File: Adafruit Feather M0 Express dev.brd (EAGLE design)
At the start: 50.8 x 22.9 mm, 41 parts, among them J2 AVR_SPI_PROG_3X2PTH, SW1 SPST_TACT-KMR2, U1 2MB Flash, U2 AP2112-3.3, U3 MCP73831T-2ACI/OT, X1 JSTPH, X2 32.768, X3 microUSB, X4 2x5 0.05" SWD

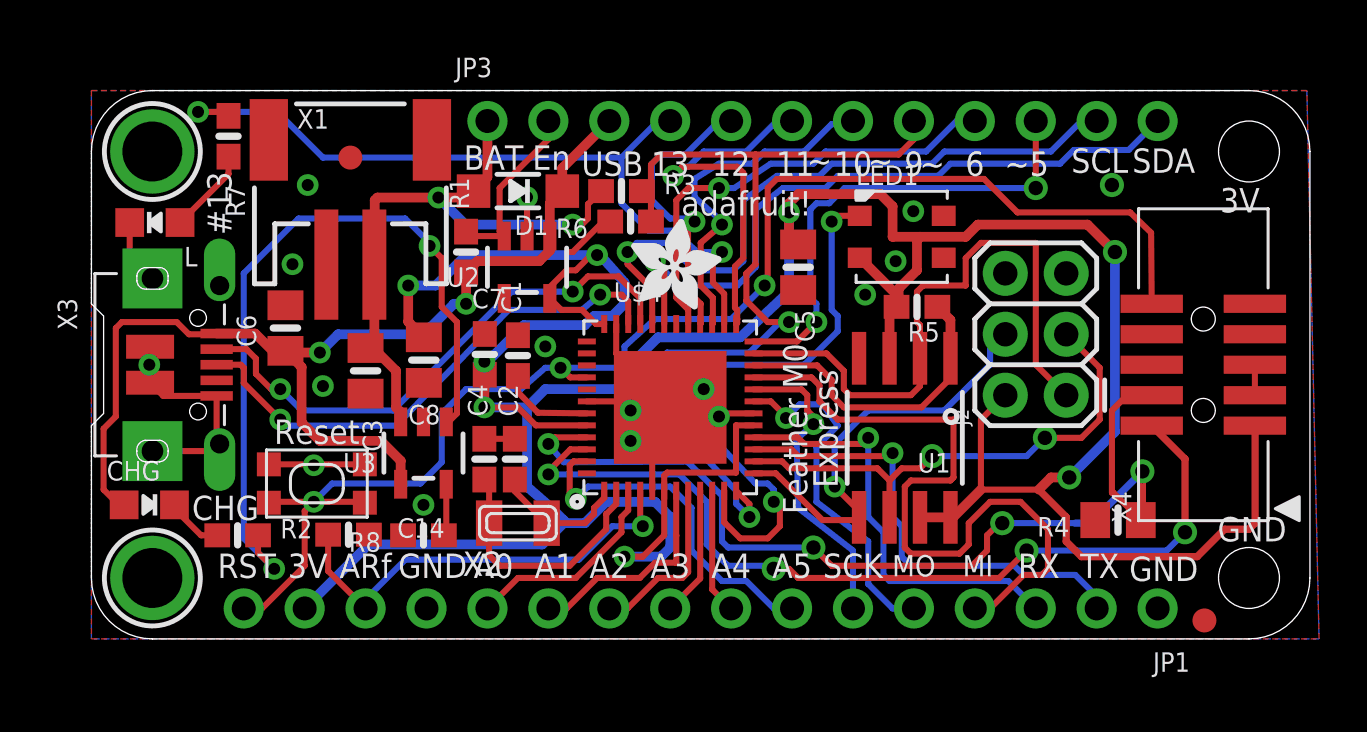
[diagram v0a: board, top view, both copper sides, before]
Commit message: fixed all bottom layer DRC errors
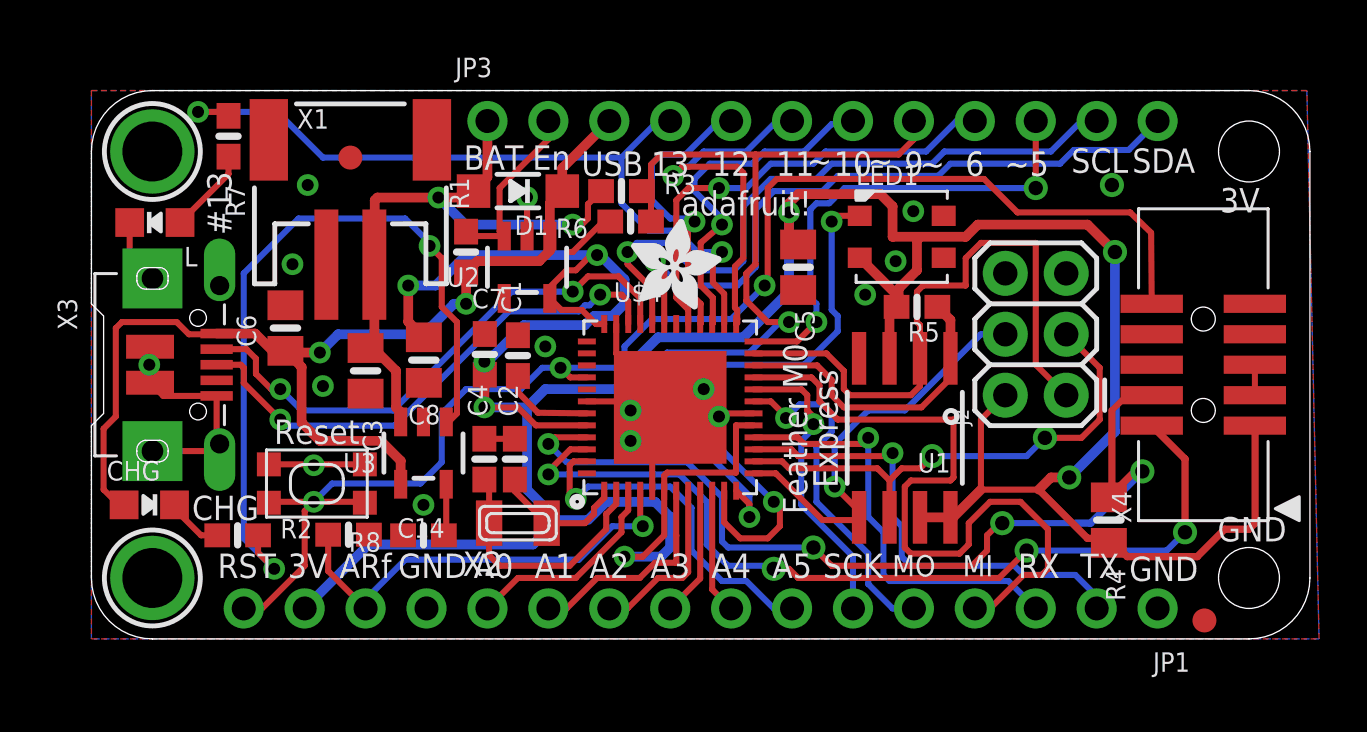
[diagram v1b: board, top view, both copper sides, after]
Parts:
- moved R4 0.38 mm to (42.4, 4.95), turned to 270 degrees
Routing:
- net SWCLK: track 40.8 -> 39.5 mm
- net +3V3: track 151.3 -> 150.3 mm

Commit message: fixed top angle DRCs. One bad overlap left
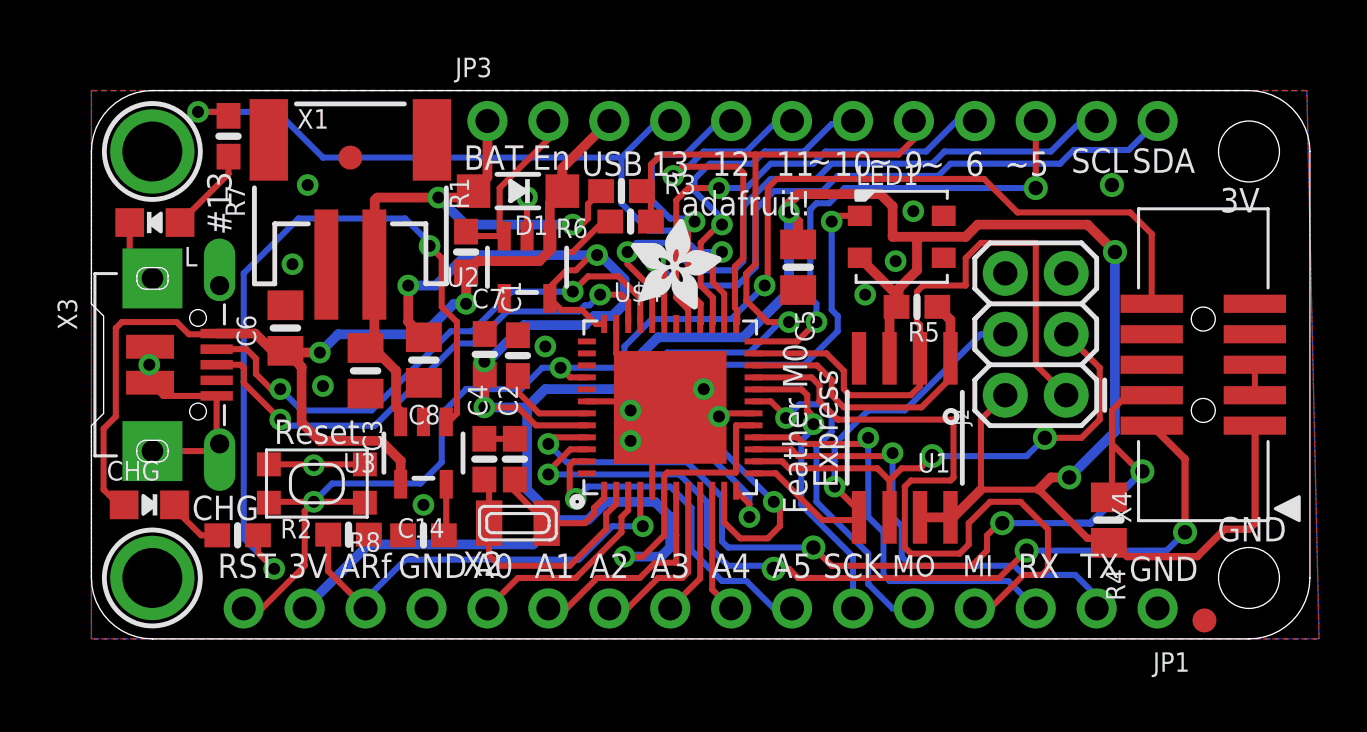
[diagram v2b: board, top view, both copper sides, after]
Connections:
- removed net 3.3V: R4.2
- net +3V3: now also R4.2
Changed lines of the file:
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@@
 <contactref element="U$4" pad="28"/>
 <via x="25.146" y="17.399" extent="1-16" drill="0.5"/>
-<wire x1="25.146" y1="17.399" x2="24.872" y2="17.165" width="0.254" layer="1"/>
 <wire x1="26.67" y1="21.59" x2="26.162" y2="21.59" width="0.254" layer="16"/>
 <wire x1="26.162" y1="21.59" x2="24.765" y2="20.193" width="0.254" layer="16"/>
@@
 <wire x1="25.4" y1="13.97" x2="25.4" y2="13.147" width="0.254" layer="1"/>
 <wire x1="25.4" y1="13.147" x2="25.38" y2="13.127" width="0.254" layer="1"/>
+<wire x1="25.146" y1="17.399" x2="24.912" y2="17.165" width="0.254" layer="1"/>
+<wire x1="24.912" y1="17.165" x2="24.872" y2="17.165" width="0.254" layer="1"/>
 </signal>
 <signal name="+3V3">
@@
 <wire x1="23.88" y1="6.8112" x2="24.003" y2="6.9342" width="0.254" layer="1"/>
 <via x="29.083" y="17.78" extent="1-16" drill="0.5"/>
-<wire x1="29.083" y1="17.78" x2="29.083" y2="16.764" width="0.4064" layer="1"/>
-<wire x1="29.083" y1="16.764" x2="29.464" y2="16.444" width="0.4064" layer="1"/>
 <wire x1="21.209" y1="16.002" x2="21.082" y2="16.002" width="0.254" layer="16"/>
 <wire x1="14.351" y1="14.732" x2="13.208" y2="14.732" width="0.4064" layer="16"/>
@@
 <wire x1="35.814" y1="5.067" x2="34.544" y2="5.067" width="0.4064" layer="1"/>
 <contactref element="R5" pad="2"/>
-<wire x1="29.083" y1="17.78" x2="29.083" y2="18.161" width="0.4064" layer="1"/>
+<wire x1="29.083" y1="18.161" x2="29.083" y2="17.78" width="0.4064" layer="1"/>
 <wire x1="29.083" y1="18.161" x2="29.464" y2="18.542" width="0.4064" layer="1"/>
 <wire x1="29.464" y1="18.542" x2="32.893" y2="18.542" width="0.4064" layer="1"/>
@@
 <wire x1="41.529" y1="4.191" x2="39.497" y2="6.223" width="0.3048" layer="1"/>
 <wire x1="19.431" y1="4.953" x2="18.161" y2="6.223" width="0.4064" layer="16"/>
-<wire x1="20.574" y1="4.953" x2="20.701" y2="4.953" width="0" layer="19" extent="16-16"/>
+<wire x1="29.083" y1="17.78" x2="29.464" y2="17.399" width="0.4064" layer="1"/>
+<wire x1="29.464" y1="17.399" x2="29.464" y2="16.444" width="0.4064" layer="1"/>
+<contactref element="R4" pad="2"/>
+<wire x1="42.418" y1="4.191" x2="42.418" y2="4.003" width="0" layer="19" extent="1-1"/>
+<wire x1="20.701" y1="4.953" x2="20.574" y2="4.953" width="0" layer="19" extent="16-16"/>
 </signal>
 <signal name="VBUS">
@@
 <contactref element="U$4" pad="43"/>
 <contactref element="C1" pad="1"/>
-<wire x1="20.655" y1="9.402" x2="18.6182" y2="9.4274" width="0.254" layer="1"/>
-<wire x1="18.6182" y1="9.4274" x2="17.78" y2="10.287" width="0.254" layer="1"/>
+<wire x1="20.655" y1="9.402" x2="18.665" y2="9.402" width="0.254" layer="1"/>
+<wire x1="18.665" y1="9.402" x2="17.78" y2="10.287" width="0.254" layer="1"/>
 <wire x1="17.78" y1="10.287" x2="17.78" y2="10.961" width="0.254" layer="1"/>
 </signal>
@@
 <wire x1="30.861" y1="21.463" x2="31.623" y2="21.463" width="0.254" layer="16"/>
 <wire x1="31.623" y1="21.463" x2="31.75" y2="21.59" width="0.254" layer="16"/>
-<wire x1="26.289" y1="17.272" x2="25.4" y2="16.51" width="0.254" layer="1"/>
-<wire x1="25.4" y1="16.51" x2="25.4" y2="14.732" width="0.254" layer="1"/>
+<wire x1="25.4" y1="14.732" x2="25.4" y2="16.51" width="0.254" layer="1"/>
 <wire x1="25.4" y1="14.732" x2="25.908" y2="14.224" width="0.254" layer="1"/>
 <wire x1="25.908" y1="14.224" x2="25.908" y2="13.155" width="0.254" layer="1"/>
@@
 <wire x1="26.289" y1="17.526" x2="26.289" y2="17.272" width="0.254" layer="16"/>
 <wire x1="25.146" y1="18.669" x2="26.289" y2="17.526" width="0.254" layer="16"/>
+<wire x1="25.4" y1="16.51" x2="26.162" y2="17.272" width="0.254" layer="1"/>
+<wire x1="26.162" y1="17.272" x2="26.289" y2="17.272" width="0.254" layer="1"/>
 </signal>
 <signal name="D+">
@@
 <via x="7.874" y="9.144" extent="1-16" drill="0.5"/>
 <wire x1="7.874" y1="9.144" x2="8.128" y2="8.89" width="0.254" layer="16"/>
-<wire x1="12.6365" y1="8.89" x2="8.128" y2="8.89" width="0.254" layer="16"/>
+<wire x1="11.811" y1="8.89" x2="11.7475" y2="8.89" width="0.254" layer="16"/>
+<wire x1="11.7475" y1="8.89" x2="8.128" y2="8.89" width="0.254" layer="16"/>
 <wire x1="21.209" y1="14.351" x2="20.7645" y2="13.9065" width="0.254" layer="16"/>
 <via x="21.209" y="14.351" extent="1-16" drill="0.5"/>
@@
 <wire x1="20.7645" y1="13.9065" x2="20.574" y2="13.9065" width="0.254" layer="16"/>
 <wire x1="20.574" y1="13.9065" x2="20.32" y2="13.6525" width="0.254" layer="16"/>
-<wire x1="20.32" y1="13.6525" x2="17.399" y2="13.6525" width="0.254" layer="16"/>
-<wire x1="17.399" y1="13.6525" x2="12.6365" y2="8.89" width="0.254" layer="16"/>
+<wire x1="17.3355" y1="13.6525" x2="16.002" y2="12.319" width="0.254" layer="16"/>
+<wire x1="16.002" y1="12.319" x2="15.24" y2="12.319" width="0.254" layer="16"/>
+<wire x1="15.24" y1="12.319" x2="11.811" y2="8.89" width="0.254" layer="16"/>
+<wire x1="20.32" y1="13.6525" x2="17.3355" y2="13.6525" width="0.254" layer="16"/>
 </signal>
 <signal name="D-">
@@
 <via x="7.874" y="10.414" extent="1-16" drill="0.5"/>
 <wire x1="7.874" y1="10.414" x2="8.763" y2="9.525" width="0.254" layer="16"/>
-<wire x1="8.763" y1="9.525" x2="12.573" y2="9.525" width="0.254" layer="16"/>
-<wire x1="12.573" y1="9.525" x2="17.526" y2="14.478" width="0.254" layer="16"/>
-<wire x1="17.526" y1="14.478" x2="20.066" y2="14.478" width="0.254" layer="16"/>
+<wire x1="8.763" y1="9.525" x2="11.684" y2="9.525" width="0.254" layer="16"/>
+<wire x1="20.066" y1="14.478" x2="17.526" y2="14.478" width="0.254" layer="16"/>
 <via x="20.066" y="14.478" extent="1-16" drill="0.5"/>
 <wire x1="20.066" y1="14.478" x2="20.701" y2="15.113" width="0.254" layer="1"/>
@@
 <wire x1="21.971" y1="15.113" x2="22.88" y2="14.204" width="0.254" layer="1"/>
 <wire x1="22.88" y1="14.204" x2="22.88" y2="13.127" width="0.254" layer="1"/>
+<wire x1="17.526" y1="14.478" x2="15.875" y2="12.827" width="0.254" layer="16"/>
+<wire x1="15.875" y1="12.827" x2="14.986" y2="12.827" width="0.254" layer="16"/>
+<wire x1="14.986" y1="12.827" x2="11.684" y2="9.525" width="0.254" layer="16"/>
 </signal>
 <signal name="!RESET">
@@
 <wire x1="28.575" y1="19.177" x2="37.211" y2="19.177" width="0.254" layer="1"/>
 <wire x1="37.211" y1="19.177" x2="38.608" y2="17.78" width="0.254" layer="1"/>
-<wire x1="38.608" y1="17.78" x2="43.307" y2="17.78" width="0.254" layer="1"/>
-<wire x1="44.1796" y1="16.9328" x2="44.205" y2="13.97" width="0.254" layer="1"/>
-<wire x1="43.307" y1="17.78" x2="44.1796" y2="16.9328" width="0.254" layer="1"/>
+<wire x1="43.307" y1="17.78" x2="38.608" y2="17.78" width="0.254" layer="1"/>
 <wire x1="23.368" y1="13.335" x2="22.225" y2="12.192" width="0.254" layer="16"/>
 <wire x1="26.67" y1="13.335" x2="23.368" y2="13.335" width="0.254" layer="16"/>
 <wire x1="18.796" y1="11.303" x2="17.907" y2="10.414" width="0.254" layer="16"/>
 <wire x1="19.558" y1="11.303" x2="18.796" y2="11.303" width="0.254" layer="16"/>
+<wire x1="44.205" y1="13.97" x2="44.205" y2="16.882" width="0.254" layer="1"/>
+<wire x1="44.205" y1="16.882" x2="43.307" y2="17.78" width="0.254" layer="1"/>
 </signal>
 <signal name="SWCLK">
@@
 <wire x1="19.812" y1="7.366" x2="24.84755" y2="7.366" width="0.254" layer="16"/>
 <wire x1="44.205" y1="10.16" x2="43.18" y2="10.16" width="0.254" layer="1"/>
-<wire x1="43.18" y1="10.16" x2="42.545" y2="9.525" width="0.254" layer="1"/>
+<wire x1="42.545" y1="9.525" x2="43.18" y2="10.16" width="0.254" layer="1"/>
 <wire x1="37.973" y1="4.826" x2="41.021" y2="4.826" width="0.254" layer="16"/>
 <wire x1="42.545" y1="6.096" x2="42.606" y2="6.096" width="0.254" layer="1"/>
-<wire x1="42.418" y1="5.903" x2="42.606" y2="6.096" width="0.254" layer="1"/>
 <wire x1="41.021" y1="4.826" x2="41.656" y2="4.826" width="0.3048" layer="16"/>
 <wire x1="41.656" y1="4.826" x2="43.815" y2="6.985" width="0.3048" layer="16"/>
-<wire x1="42.545" y1="9.525" x2="42.545" y2="6.03" width="0.3048" layer="1"/>
-<wire x1="42.545" y1="6.03" x2="42.418" y2="5.903" width="0.3048" layer="1"/>
-<wire x1="43.815" y1="6.985" x2="43.5" y2="6.985" width="0.3048" layer="1"/>
-<wire x1="43.5" y1="6.985" x2="42.418" y2="5.903" width="0.3048" layer="1"/>
+<wire x1="42.418" y1="5.903" x2="42.545" y2="6.03" width="0.3048" layer="1"/>
+<wire x1="43.5" y1="6.985" x2="43.815" y2="6.985" width="0.3048" layer="1"/>
 <wire x1="24.84755" y1="7.366" x2="24.84755" y2="7.35965" width="0.254" layer="16"/>
 <wire x1="24.84755" y1="7.35965" x2="26.289" y2="5.9182" width="0.254" layer="16"/>
+<wire x1="43.815" y1="6.985" x2="43.688" y2="6.985" width="0.254" layer="1"/>
+<wire x1="43.688" y1="6.985" x2="42.545" y2="8.128" width="0.254" layer="1"/>
+<wire x1="42.545" y1="8.128" x2="42.545" y2="9.525" width="0.254" layer="1"/>
+<wire x1="42.545" y1="8.128" x2="42.545" y2="6.03" width="0.254" layer="1"/>
+<wire x1="42.545" y1="6.03" x2="42.418" y2="5.903" width="0.254" layer="1"/>
+<wire x1="42.545" y1="6.03" x2="42.545" y2="6.096" width="0" layer="19" extent="1-1"/>
 </signal>
 <signal name="SWDIO">
@@
 <wire x1="39.37" y1="11.43" x2="40.64" y2="10.16" width="0.254" layer="1"/>
 </signal>
-<signal name="3.3V">
-<contactref element="R4" pad="2"/>
-</signal>
 </signals>
